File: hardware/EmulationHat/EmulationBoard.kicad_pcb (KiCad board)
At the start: 4 copper layers, 28 x 25 mm, 1 part, among them U1 ATmega32U4-M

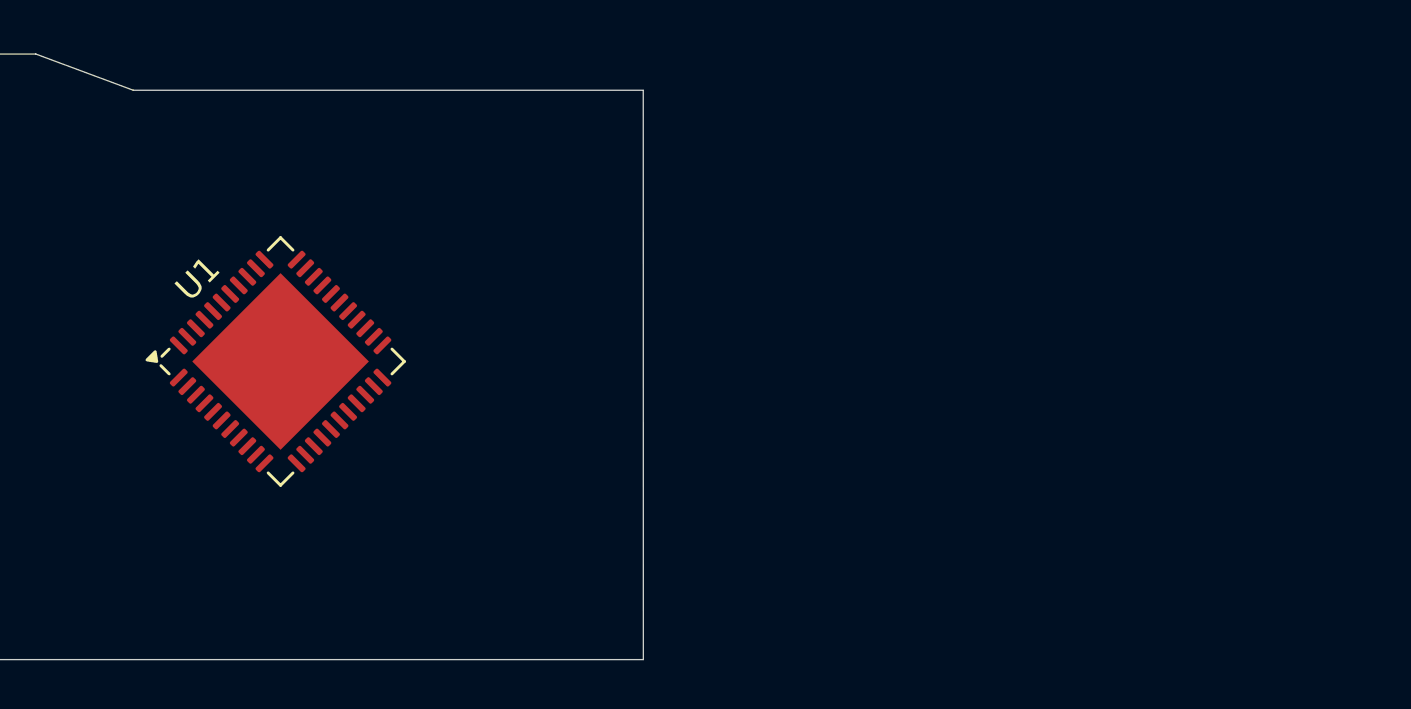
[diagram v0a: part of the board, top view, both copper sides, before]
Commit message: started adding subsystems for the emulation hat
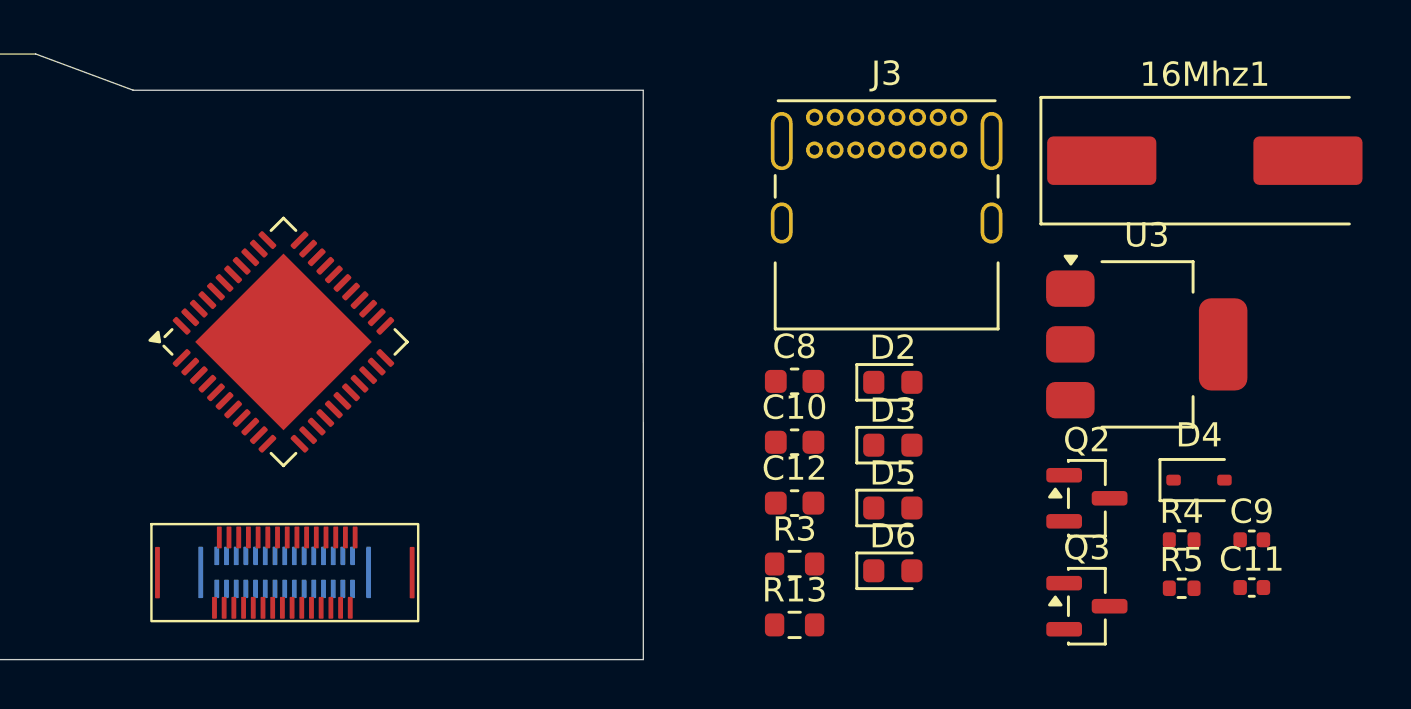
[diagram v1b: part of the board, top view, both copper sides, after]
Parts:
- added 16Mhz1: Crystal, Crystal:Crystal_SMD_HC49-SD, F.Cu at (179.5, 99.3)
- added C10: 10uF, Capacitor_SMD:C_0603_1608Metric, F.Cu at (162.6, 110.9)
- added C11: 0u1F, Capacitor_SMD:C_0402_1005Metric, F.Cu at (181.4, 116.9)
- added C12: 10uF, Capacitor_SMD:C_0603_1608Metric, F.Cu at (162.6, 113.4)
- added C8: 10uF, Capacitor_SMD:C_0603_1608Metric, F.Cu at (162.6, 108.4)
- added C9: 0u1F, Capacitor_SMD:C_0402_1005Metric, F.Cu at (181.4, 115.0)
- added D2: PWRLED, LED_SMD:LED_0603_1608Metric, F.Cu at (166.7, 108.5)
- added D3: D_TVS_Small_Filled, Diode_SMD:D_0603_1608Metric, F.Cu at (166.7, 111.0)
- added D4: 1N5819WS, Diode_SMD:D_SOD-323, F.Cu at (179.3, 112.5)
- added D5: D_TVS_Small_Filled, Diode_SMD:D_0603_1608Metric, F.Cu at (166.7, 113.6)
- added D6: D_TVS_Small_Filled, Diode_SMD:D_0603_1608Metric, F.Cu at (166.7, 116.2)
- added J1: Conn_02x16_Top_Bottom, MolexFSB:FSB5 Series 0.40 mm Pitch Floating SlimStack Board-to-Board Receptacles, B.Cu at (141.6, 116.3)
- added J2: Conn_02x16_Top_Bottom, MolexFSB:FSB5 Series 0.40 mm Pitch Floating SlimStack Board-to-Board Plugs, F.Cu at (141.6, 116.3)
- added J3: USB_C_Receptacle_USB2.0_16P, Connector_USB:USB_C_Receptacle_GCT_USB4085, F.Cu at (163.4, 97.5)
- added Q2: FDN340P, Package_TO_SOT_SMD:SOT-23, F.Cu at (174.7, 113.2)
- added Q3: FDN340P, Package_TO_SOT_SMD:SOT-23, F.Cu at (174.7, 117.7)
- added R13: 10K, Resistor_SMD:R_0603_1608Metric, F.Cu at (162.6, 118.5)
- added R3: 75, Resistor_SMD:R_0603_1608Metric, F.Cu at (162.6, 116.0)
- added R4: 5k1, Resistor_SMD:R_0402_1005Metric, F.Cu at (178.6, 115.0)
- added R5: 5k1, Resistor_SMD:R_0402_1005Metric, F.Cu at (178.6, 117.0)
- added U3: AMS1117-5.0, Package_TO_SOT_SMD:SOT-223-3_TabPin2, F.Cu at (177.1, 106.9)
- moved U1 0.82 mm to (141.5, 106.8)

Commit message: more emulation hat stuff
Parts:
- removed 16Mhz1: Crystal, Crystal:Crystal_SMD_HC49-SD
- removed C10, C12, C8: 10uF, Capacitor_SMD:C_0603_1608Metric
- removed C11, C9: 0u1F, Capacitor_SMD:C_0402_1005Metric
- removed D2: PWRLED, LED_SMD:LED_0603_1608Metric
- removed D3, D5, D6: D_TVS_Small_Filled, Diode_SMD:D_0603_1608Metric
- removed D4: 1N5819WS, Diode_SMD:D_SOD-323
- removed J3: USB_C_Receptacle_USB2.0_16P, Connector_USB:USB_C_Receptacle_GCT_USB4085
- removed Q2, Q3: FDN340P, Package_TO_SOT_SMD:SOT-23
- removed R13: 10K, Resistor_SMD:R_0603_1608Metric
- removed R3: 75, Resistor_SMD:R_0603_1608Metric
- removed R4, R5: 5k1, Resistor_SMD:R_0402_1005Metric
- removed U1: ATmega32U4-M, Package_DFN_QFN:QFN-44-1EP_7x7mm_P0.5mm_EP5.15x5.15mm
- removed U3: AMS1117-5.0, Package_TO_SOT_SMD:SOT-223-3_TabPin2
- turned J1 to 0 degrees
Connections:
- J1 pad 31: unconnected-(J1-Pin_31-Pad31) -> VIN
- J2 pad 31: unconnected-(J2-Pin_31-Pad31) -> VIN
- J2 pad 32: unconnected-(J2-Pin_32-Pad32) -> GND
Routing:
- net GND: track 0.00 -> 1.80 mm, vias 0 -> 1
- net VIN: track 0.00 -> 1.79 mm, vias 0 -> 1

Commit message: emulation
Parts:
- added C10: 10uF, Capacitor_SMD:C_0603_1608Metric, F.Cu at (160.4, 111.0)
- added C11: 0u1F, Capacitor_SMD:C_0402_1005Metric, F.Cu at (179.3, 117.0)
- added C14: 10uF, Capacitor_SMD:C_0603_1608Metric, F.Cu at (160.4, 113.5)
- added C8: 10uF, Capacitor_SMD:C_0603_1608Metric, F.Cu at (160.4, 108.5)
- added C9: 0u1F, Capacitor_SMD:C_0402_1005Metric, F.Cu at (179.3, 115.0)
- added D1: PWRLED, LED_SMD:LED_0603_1608Metric, F.Cu at (164.5, 108.6)
- added D2: D_TVS_Small_Filled, Diode_SMD:D_0603_1608Metric, F.Cu at (164.5, 111.2)
- added D3: 1N5819WS, Diode_SMD:D_SOD-323, F.Cu at (177.1, 112.5)
- added D4: D_TVS_Small_Filled, Diode_SMD:D_0603_1608Metric, F.Cu at (164.5, 113.7)
- added D5: D_TVS_Small_Filled, Diode_SMD:D_0603_1608Metric, F.Cu at (164.5, 116.3)
- added J5: USB_C_Receptacle_USB2.0_16P, Connector_USB:USB_C_Receptacle_GCT_USB4085, F.Cu at (161.3, 97.6)
- added Q2: FDN340P, Package_TO_SOT_SMD:SOT-23, F.Cu at (172.5, 113.3)
- added Q3: FDN340P, Package_TO_SOT_SMD:SOT-23, F.Cu at (172.5, 117.8)
- added R10: 5k1, Resistor_SMD:R_0402_1005Metric, F.Cu at (176.4, 117.0)
- added R13: 10K, Resistor_SMD:R_0603_1608Metric, F.Cu at (160.4, 118.6)
- added R3: 75, Resistor_SMD:R_0603_1608Metric, F.Cu at (160.4, 116.0)
- added R9: 5k1, Resistor_SMD:R_0402_1005Metric, F.Cu at (176.4, 115.0)
- added U3: AMS1117-5.0, Package_TO_SOT_SMD:SOT-223-3_TabPin2, F.Cu at (175.0, 107.0)

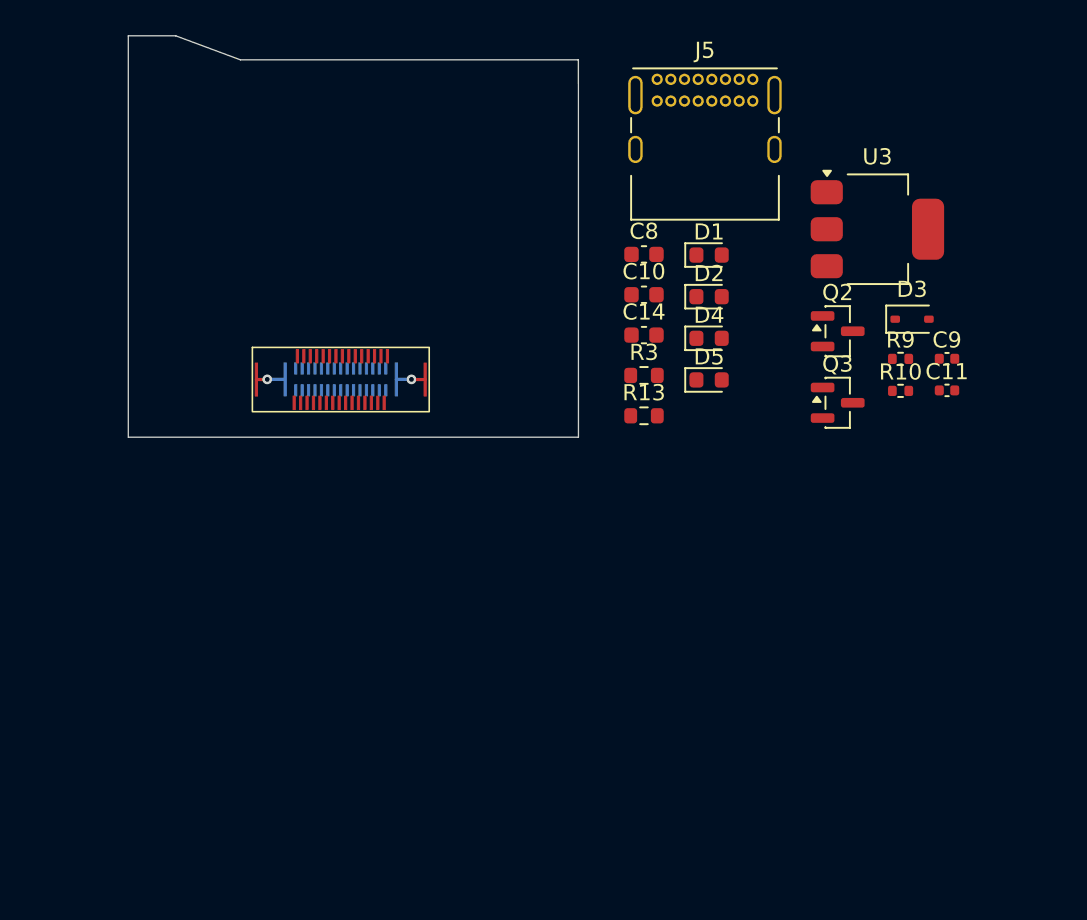
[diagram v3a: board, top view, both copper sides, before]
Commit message: correct connector placement
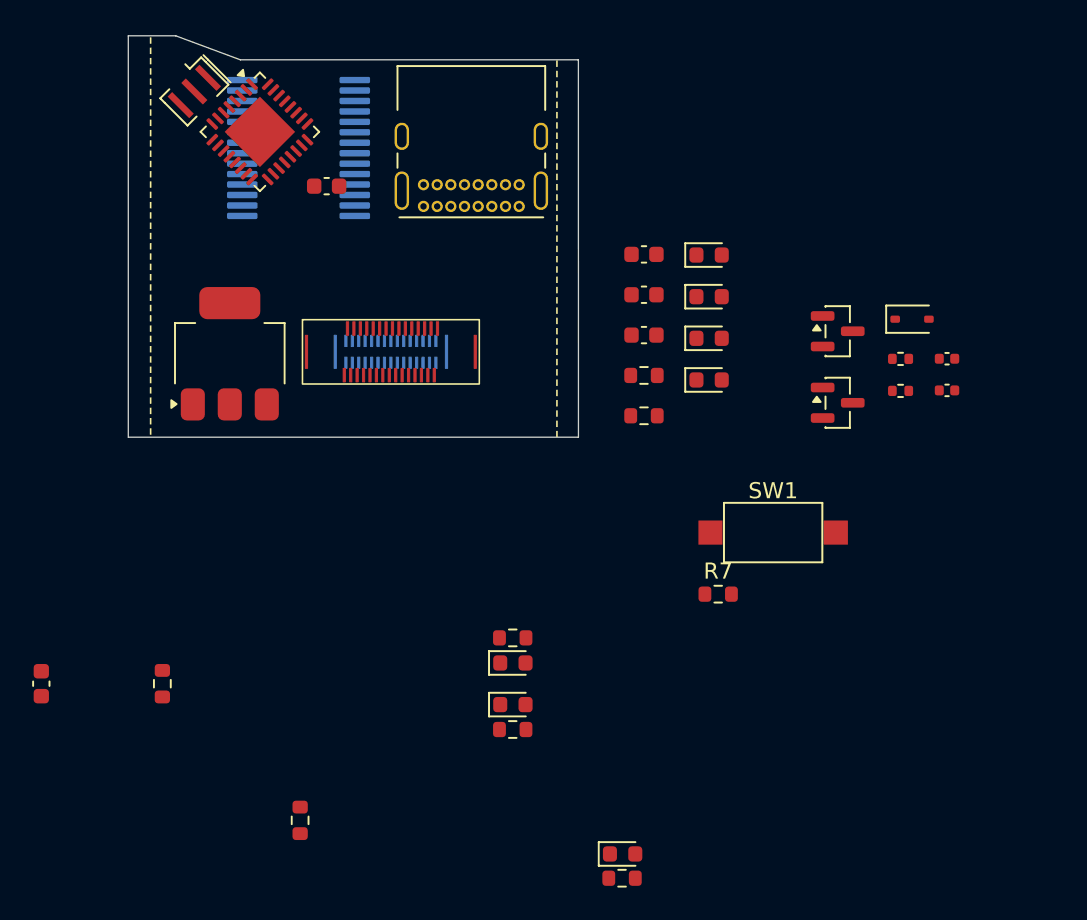
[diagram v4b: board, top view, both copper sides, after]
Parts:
- added C1: 100nF, Capacitor_SMD:C_0603_1608Metric, F.Cu at (140.7, 104.3)
- added C2: 100nF, Capacitor_SMD:C_0603_1608Metric, F.Cu at (123.0, 135.2)
- added D6: TXLED, LED_SMD:LED_0603_1608Metric, F.Cu at (152.3, 133.9)
- added D7: RXLED, LED_SMD:LED_0603_1608Metric, F.Cu at (152.3, 136.5)
- added D8: LED, LED_SMD:LED_0603_1608Metric, F.Cu at (159.1, 145.8)
- added R1: 1k, Resistor_SMD:R_0603_1608Metric, F.Cu at (152.3, 132.4)
- added R2: 1k, Resistor_SMD:R_0603_1608Metric, F.Cu at (152.3, 138.1)
- added R4: 1k, Resistor_SMD:R_0603_1608Metric, F.Cu at (130.5, 135.2)
- added R5: 1k, Resistor_SMD:R_0603_1608Metric, F.Cu at (139.1, 143.7)
- added R6: 1k, Resistor_SMD:R_0603_1608Metric, F.Cu at (159.1, 147.3)
- added R7: 1k, Resistor_SMD:R_0603_1608Metric, F.Cu at (165.1, 129.7)
- added SW1: SW_Push, Button_Switch_SMD:SW_SPST_CK_RS282G05A3, F.Cu at (168.5, 125.8)
- added U1: ATmega328P-M, Package_DFN_QFN:QFN-32-1EP_5x5mm_P0.5mm_EP3.1x3.1mm, F.Cu at (136.5, 100.9)
- added U2: FT232RL, Package_SO:SSOP-28_5.3x10.2mm_P0.65mm, B.Cu at (138.9, 101.9)
- added Y2: Resonator, Crystal:Resonator_SMD_Murata_CSTxExxV-3Pin_3.0x1.1mm, F.Cu at (132.5, 98.4)
- moved U3 41.0 mm to (134.7, 114.7), turned to 90 degrees
- moved J5 11.7 mm to (152.7, 105.5), turned to 180 degrees
- moved J2 3.56 mm to (144.7, 114.6)
- moved J1 3.56 mm to (144.7, 114.6)
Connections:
- C10 pad 1: VCC_5V -> +5V
- C11 pad 1: VCC_5V -> +5V
- C14 pad 1: VUSB -> VBUS
- D3 pad 1: VUSB -> VBUS
- J1 pad 1: unconnected-(J1-Pin_1-Pad1) -> CONN_0
- J1 pad 10: unconnected-(J1-Pin_10-Pad10) -> CONN_9
- J1 pad 11: unconnected-(J1-Pin_11-Pad11) -> CONN_10
- J1 pad 12: unconnected-(J1-Pin_12-Pad12) -> CONN_11
- J1 pad 13: unconnected-(J1-Pin_13-Pad13) -> CONN_12
- J1 pad 14: unconnected-(J1-Pin_14-Pad14) -> CONN_13
- J1 pad 15: unconnected-(J1-Pin_15-Pad15) -> CONN_14
- J1 pad 16: unconnected-(J1-Pin_16-Pad16) -> CONN_15
- J1 pad 17: unconnected-(J1-Pin_17-Pad17) -> CONN_16
- J1 pad 18: unconnected-(J1-Pin_18-Pad18) -> CONN_17
- J1 pad 19: unconnected-(J1-Pin_19-Pad19) -> CONN_18
- J1 pad 2: unconnected-(J1-Pin_2-Pad2) -> CONN_1
- J1 pad 20: unconnected-(J1-Pin_20-Pad20) -> CONN_19
- J1 pad 21: unconnected-(J1-Pin_21-Pad21) -> CONN_20
- J1 pad 22: unconnected-(J1-Pin_22-Pad22) -> CONN_21
- J1 pad 23: unconnected-(J1-Pin_23-Pad23) -> CONN_22
- J1 pad 24: unconnected-(J1-Pin_24-Pad24) -> CONN_23
- J1 pad 25: unconnected-(J1-Pin_25-Pad25) -> CONN_24
- J1 pad 26: unconnected-(J1-Pin_26-Pad26) -> CONN_25
- J1 pad 27: unconnected-(J1-Pin_27-Pad27) -> CONN_26
- J1 pad 28: unconnected-(J1-Pin_28-Pad28) -> CONN_27
- J1 pad 29: unconnected-(J1-Pin_29-Pad29) -> CONN_28
- J1 pad 3: unconnected-(J1-Pin_3-Pad3) -> CONN_2
- J1 pad 30: unconnected-(J1-Pin_30-Pad30) -> CONN_29
- J1 pad 4: unconnected-(J1-Pin_4-Pad4) -> CONN_3
- J1 pad 5: unconnected-(J1-Pin_5-Pad5) -> CONN_4
- J1 pad 6: unconnected-(J1-Pin_6-Pad6) -> CONN_5
- J1 pad 7: unconnected-(J1-Pin_7-Pad7) -> CONN_6
- J1 pad 8: unconnected-(J1-Pin_8-Pad8) -> CONN_7
- J1 pad 9: unconnected-(J1-Pin_9-Pad9) -> CONN_8
- J2 pad 1: unconnected-(J2-Pin_1-Pad1) -> CONN_15
- J2 pad 10: unconnected-(J2-Pin_10-Pad10) -> CONN_24
- J2 pad 11: unconnected-(J2-Pin_11-Pad11) -> CONN_25
- J2 pad 12: unconnected-(J2-Pin_12-Pad12) -> CONN_26
- J2 pad 13: unconnected-(J2-Pin_13-Pad13) -> CONN_27
- J2 pad 14: unconnected-(J2-Pin_14-Pad14) -> CONN_28
- J2 pad 15: unconnected-(J2-Pin_15-Pad15) -> CONN_29
- J2 pad 16: unconnected-(J2-Pin_16-Pad16) -> CONN_0
- J2 pad 17: unconnected-(J2-Pin_17-Pad17) -> CONN_1
- J2 pad 18: unconnected-(J2-Pin_18-Pad18) -> CONN_2
- J2 pad 19: unconnected-(J2-Pin_19-Pad19) -> CONN_3
- J2 pad 2: unconnected-(J2-Pin_2-Pad2) -> CONN_16
- J2 pad 20: unconnected-(J2-Pin_20-Pad20) -> CONN_4
- J2 pad 21: unconnected-(J2-Pin_21-Pad21) -> CONN_5
- J2 pad 22: unconnected-(J2-Pin_22-Pad22) -> CONN_6
- J2 pad 23: unconnected-(J2-Pin_23-Pad23) -> CONN_7
- J2 pad 24: unconnected-(J2-Pin_24-Pad24) -> CONN_8
- J2 pad 25: unconnected-(J2-Pin_25-Pad25) -> CONN_9
- J2 pad 26: unconnected-(J2-Pin_26-Pad26) -> CONN_10
- J2 pad 27: unconnected-(J2-Pin_27-Pad27) -> CONN_11
- J2 pad 28: unconnected-(J2-Pin_28-Pad28) -> CONN_12
- J2 pad 29: unconnected-(J2-Pin_29-Pad29) -> CONN_13
- J2 pad 3: unconnected-(J2-Pin_3-Pad3) -> CONN_17
- J2 pad 30: unconnected-(J2-Pin_30-Pad30) -> CONN_14
- J2 pad 4: unconnected-(J2-Pin_4-Pad4) -> CONN_18
- J2 pad 5: unconnected-(J2-Pin_5-Pad5) -> CONN_19
- J2 pad 6: unconnected-(J2-Pin_6-Pad6) -> CONN_20
- J2 pad 7: unconnected-(J2-Pin_7-Pad7) -> CONN_21
- J2 pad 8: unconnected-(J2-Pin_8-Pad8) -> CONN_22
- J2 pad 9: unconnected-(J2-Pin_9-Pad9) -> CONN_23
- R3 pad 1: VCC_5V -> +5V
- U3 pad 2: VCC_5V -> +5V
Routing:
- net GND: track 1.80 -> 0.00 mm, vias 1 -> 0
- net VIN: track 1.79 -> 0.00 mm, vias 1 -> 0

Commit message: emulation hat and stuff
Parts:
- R4, R5: moved to B.Cu
- moved C2 41.6 mm to (164.6, 135.7), turned to 0 degrees
- moved R5 40.2 mm to (131.0, 104.3)
- moved R4 27.9 mm to (131.0, 107.4)
- moved SW1 9.96 mm to (171.0, 135.4), turned to 180 degrees
- moved D8 8.72 mm to (152.2, 140.5)
- moved R6 8.72 mm to (152.2, 142.0)
- moved R7 4.52 mm to (164.6, 134.2)
